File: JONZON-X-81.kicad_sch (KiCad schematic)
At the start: 30 parts, among them SW1 SW_DIP_x03, U1 AY-3-8910, U2 74HCT74, U3 74HCT08, U4 74HCT11, U5 74HCT02

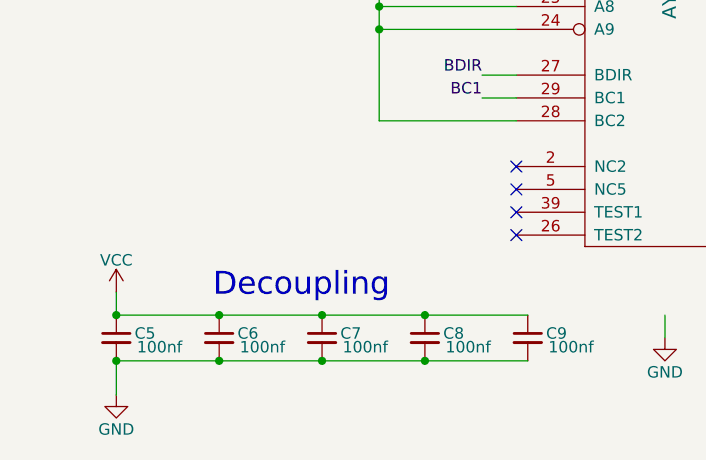
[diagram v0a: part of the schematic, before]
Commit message: Renamed files Added Ground and Audio Ground Planes Moved Ground Bridge to be between ground planes Generated some new images
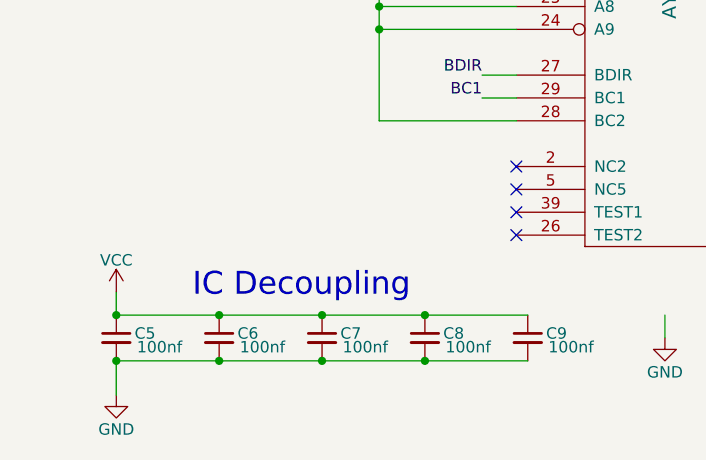
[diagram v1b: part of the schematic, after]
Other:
- note added: "IC Decoupling"
- note removed: "Decoupling"
- title: JonZON-X -> JONZON-X-81
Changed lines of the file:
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@@
 	(paper "A4")
 	(title_block
-		(title "JonZON-X")
+		(title "JONZON-X-81")
 		(date "2025-08-01")
 		(rev "1.0")
@@
 		)
 	)
-	(text "Decoupling"
+	(text "IC Decoupling"
 		(exclude_from_sim no)
 		(at 43.434 178.308 0)

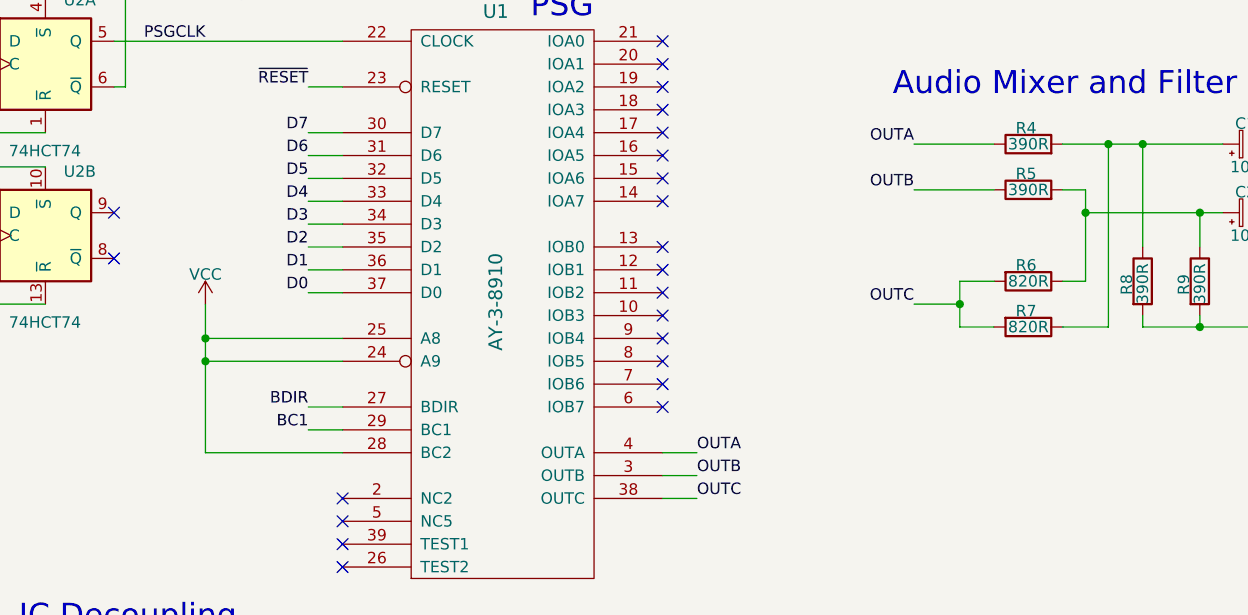
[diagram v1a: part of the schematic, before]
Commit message: Pulled /A9 low
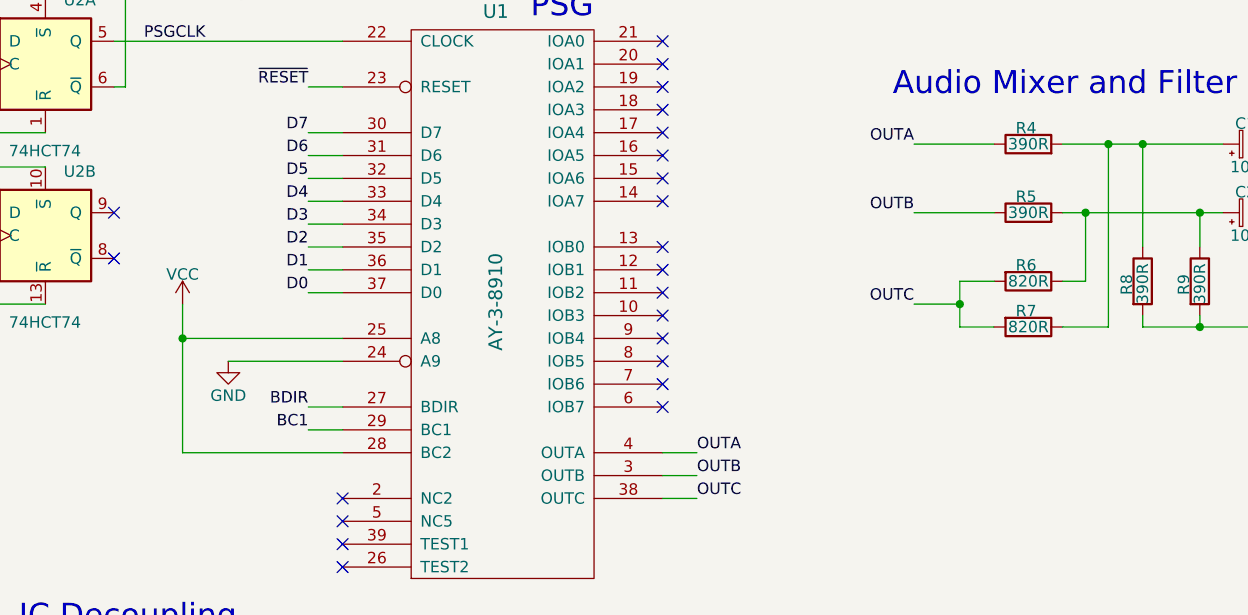
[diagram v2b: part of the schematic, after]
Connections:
- net GND: now also U1.24 (A9)
- net VCC: no longer U1.24 (A9)
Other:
- moved on the sheet: R5
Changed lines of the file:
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@@
 	)
 	(junction
-		(at 52.07 149.86)
-		(diameter 0)
-		(color 0 0 0 0)
-	)
-	(junction
 		(at 260.35 121.92)
 		(diameter 0)
@@
 	)
 	(junction
-		(at 52.07 147.32)
-		(diameter 0)
-		(color 0 0 0 0)
-	)
-	(junction
 		(at 90.17 31.75)
 		(diameter 0)
@@
 	)
 	(junction
+		(at 49.53 147.32)
+		(diameter 0)
+		(color 0 0 0 0)
+	)
+	(junction
 		(at 24.13 135.89)
 		(diameter 0)
@@
 	(wire
 		(pts
-			(xy 69.85 82.55) (xy 64.77 82.55)
+			(xy 54.61 149.86) (xy 67.31 149.86)
 		)
 		(stroke
@@
 	(wire
 		(pts
-			(xy 130.81 46.99) (xy 135.89 46.99)
+			(xy 69.85 82.55) (xy 64.77 82.55)
 		)
 		(stroke
@@
 	(wire
 		(pts
-			(xy 147.32 125.73) (xy 152.4 125.73)
+			(xy 130.81 46.99) (xy 135.89 46.99)
 		)
 		(stroke
@@
 	(wire
 		(pts
-			(xy 22.86 181.61) (xy 34.29 181.61)
+			(xy 147.32 125.73) (xy 152.4 125.73)
 		)
 		(stroke
@@
 	(wire
 		(pts
-			(xy 163.83 35.56) (xy 166.37 35.56)
+			(xy 22.86 181.61) (xy 34.29 181.61)
 		)
 		(stroke
@@
 	(wire
 		(pts
-			(xy 26.67 67.31) (xy 31.75 67.31)
+			(xy 163.83 35.56) (xy 166.37 35.56)
 		)
 		(stroke
@@
 	(wire
 		(pts
-			(xy 26.67 133.35) (xy 24.13 133.35)
+			(xy 26.67 67.31) (xy 31.75 67.31)
 		)
 		(stroke
@@
 	(wire
 		(pts
-			(xy 52.07 149.86) (xy 67.31 149.86)
+			(xy 26.67 133.35) (xy 24.13 133.35)
 		)
 		(stroke
@@
 	(wire
 		(pts
+			(xy 130.81 133.35) (xy 139.7 133.35)
+		)
+		(stroke
+			(width 0)
+			(type default)
+		)
+	)
+	(wire
+		(pts
 			(xy 162.56 133.35) (xy 165.1 133.35)
 		)
@@
 	(wire
 		(pts
-			(xy 52.07 147.32) (xy 67.31 147.32)
-		)
-		(stroke
-			(width 0)
-			(type default)
-		)
-	)
-	(wire
-		(pts
 			(xy 255.27 35.56) (xy 255.27 40.64)
 		)
@@
 	(wire
 		(pts
-			(xy 149.86 133.35) (xy 149.86 130.81)
-		)
-		(stroke
-			(width 0)
-			(type default)
-		)
-	)
-	(wire
-		(pts
 			(xy 156.21 144.78) (xy 156.21 146.05)
 		)
@@
 	(wire
 		(pts
-			(xy 52.07 147.32) (xy 52.07 149.86)
+			(xy 49.53 147.32) (xy 49.53 160.02)
 		)
 		(stroke
@@
 	(wire
 		(pts
-			(xy 52.07 160.02) (xy 67.31 160.02)
+			(xy 49.53 160.02) (xy 67.31 160.02)
 		)
 		(stroke
@@
 	(wire
 		(pts
-			(xy 130.81 130.81) (xy 139.7 130.81)
-		)
-		(stroke
-			(width 0)
-			(type default)
-		)
-	)
-	(wire
-		(pts
 			(xy 17.78 116.84) (xy 26.67 116.84)
 		)
@@
 	(wire
 		(pts
-			(xy 52.07 143.51) (xy 52.07 147.32)
+			(xy 49.53 143.51) (xy 49.53 147.32)
 		)
 		(stroke
@@
 	(wire
 		(pts
-			(xy 147.32 130.81) (xy 149.86 130.81)
+			(xy 147.32 133.35) (xy 149.86 133.35)
 		)
 		(stroke
@@
 	(wire
 		(pts
-			(xy 52.07 149.86) (xy 52.07 160.02)
+			(xy 203.2 125.73) (xy 195.58 125.73)
 		)
 		(stroke
@@
 	(wire
 		(pts
-			(xy 203.2 125.73) (xy 195.58 125.73)
+			(xy 139.7 140.97) (xy 135.89 140.97)
 		)
 		(stroke
@@
 	(wire
 		(pts
-			(xy 139.7 140.97) (xy 135.89 140.97)
+			(xy 76.2 31.75) (xy 71.12 31.75)
 		)
 		(stroke
@@
 	(wire
 		(pts
-			(xy 76.2 31.75) (xy 71.12 31.75)
+			(xy 49.53 147.32) (xy 67.31 147.32)
 		)
 		(stroke
@@
 	)
 	(label "OUTB"
-		(at 130.81 130.81 180)
+		(at 130.81 133.35 180)
 		(effects
 			(font
@@
 		(lib_name "R_6")
 		(lib_id "Device:R")
-		(at 143.51 130.81 90)
+		(at 143.51 133.35 90)
 		(unit 1)
 		(exclude_from_sim no)
@@
 		(dnp no)
 		(property "Reference" "R5"
-			(at 143.256 129.032 90)
+			(at 143.256 131.572 90)
 			(effects
 				(font
@@
 		)
 		(property "Value" "390R"
-			(at 143.51 130.81 90)
+			(at 143.51 133.35 90)
 			(effects
 				(font
@@
 		)
 		(property "Footprint" "Resistor_THT:R_Axial_DIN0207_L6.3mm_D2.5mm_P7.62mm_Horizontal"
-			(at 143.51 132.588 90)
+			(at 143.51 135.128 90)
 			(effects
 				(font
@@
 		)
 		(property "Datasheet" "~"
-			(at 143.51 130.81 0)
+			(at 143.51 133.35 0)
 			(effects
 				(font
@@
 		)
 		(property "Description" "Resistor"
-			(at 143.51 130.81 0)
+			(at 143.51 133.35 0)
 			(effects
 				(font
@@
 	(symbol
 		(lib_id "power:VCC")
-		(at 52.07 143.51 0)
+		(at 49.53 143.51 0)
 		(unit 1)
 		(exclude_from_sim no)
@@
 		(dnp no)
 		(property "Reference" "#PWR03"
-			(at 52.07 147.32 0)
+			(at 49.53 147.32 0)
 			(effects
 				(font
@@
 		)
 		(property "Value" "VCC"
-			(at 52.07 140.208 0)
+			(at 49.53 140.208 0)
 			(effects
 				(font
@@
 		)
 		(property "Footprint" ""
-			(at 52.07 143.51 0)
+			(at 49.53 143.51 0)
 			(effects
 				(font
@@
 		)
 		(property "Datasheet" ""
-			(at 52.07 143.51 0)
+			(at 49.53 143.51 0)
 			(effects
 				(font
@@
 		)
 		(property "Description" "Power symbol creates a global label with name \"VCC\""
-			(at 52.07 143.51 0)
+			(at 49.53 143.51 0)
 			(effects
 				(font
@@
 					(unit 1)
 				)
+			)
+		)
+	)
+	(symbol
+		(lib_id "power:GND")
+		(at 54.61 149.86 0)
+		(unit 1)
+		(exclude_from_sim no)
+		(in_bom yes)
+		(on_board yes)
+		(dnp no)
+		(property "Reference" "#PWR015"
+			(at 54.61 156.21 0)
+			(effects
+				(font
+					(size 1.27 1.27)
+				)
+				(hide yes)
+			)
+		)
+		(property "Value" "GND"
+			(at 54.61 153.67 0)
+			(effects
+				(font
+					(size 1.27 1.27)
+				)
+			)
+		)
+		(property "Footprint" ""
+			(at 54.61 149.86 0)
+			(effects
+				(font
+					(size 1.27 1.27)
+				)
+				(hide yes)
+			)
+		)
+		(property "Datasheet" ""
+			(at 54.61 149.86 0)
+			(effects
+				(font
+					(size 1.27 1.27)
+				)
+				(hide yes)
+			)
+		)
+		(property "Description" "Power symbol creates a global label with name \"GND\" , ground"
+			(at 54.61 149.86 0)
+			(effects
+				(font
+					(size 1.27 1.27)
+				)
+				(hide yes)
+			)
+		)
+		(pin "1"
+		)
+		(instances
+			(project "JONZON-X-81"
+				(path "/84e03406-665a-4400-b991-4fa8ce9d51c9"
+					(reference "#PWR015")
+					(unit 1)
+				)

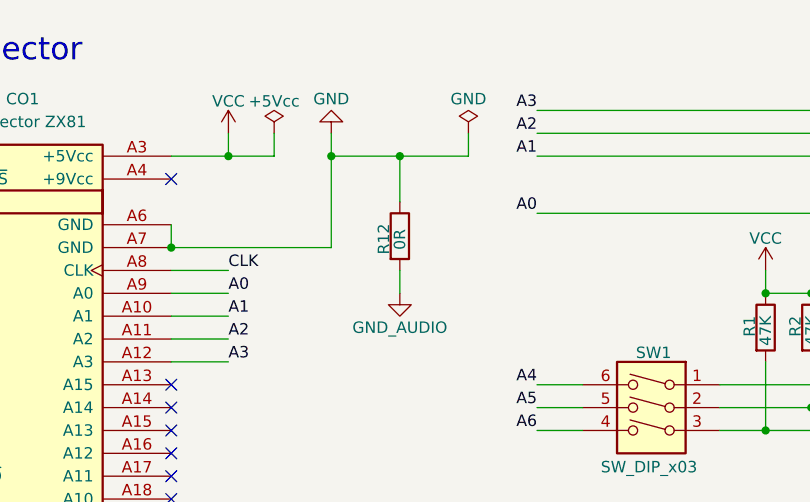
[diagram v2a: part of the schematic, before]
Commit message: fenced and stiched ground planes
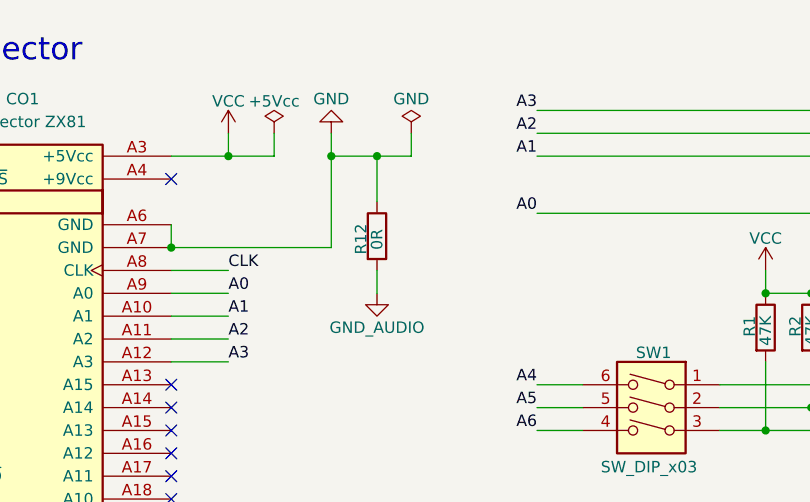
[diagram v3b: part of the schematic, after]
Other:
- moved on the sheet: R12
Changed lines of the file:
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@@
 	)
 	(junction
-		(at 260.35 121.92)
+		(at 87.63 31.75)
 		(diameter 0)
 		(color 0 0 0 0)
 	)
 	(junction
-		(at 90.17 31.75)
+		(at 260.35 121.92)
 		(diameter 0)
 		(color 0 0 0 0)
@@
 	(wire
 		(pts
-			(xy 90.17 31.75) (xy 97.79 31.75)
-		)
-		(stroke
-			(width 0)
-			(type default)
-		)
-	)
-	(wire
-		(pts
-			(xy 97.79 29.21) (xy 97.79 31.75)
+			(xy 91.44 29.21) (xy 91.44 31.75)
 		)
 		(stroke
@@
 	(wire
 		(pts
-			(xy 90.17 44.45) (xy 90.17 46.99)
-		)
-		(stroke
-			(width 0)
-			(type default)
-		)
-	)
-	(wire
-		(pts
 			(xy 43.18 106.68) (xy 43.18 119.38)
 		)
@@
 	(wire
 		(pts
-			(xy 90.17 31.75) (xy 90.17 36.83)
+			(xy 87.63 31.75) (xy 87.63 36.83)
 		)
 		(stroke
@@
 	(wire
 		(pts
+			(xy 87.63 31.75) (xy 91.44 31.75)
+		)
+		(stroke
+			(width 0)
+			(type default)
+		)
+	)
+	(wire
+		(pts
 			(xy 193.04 124.46) (xy 193.04 133.35)
 		)
@@
 	(wire
 		(pts
-			(xy 82.55 31.75) (xy 90.17 31.75)
+			(xy 82.55 31.75) (xy 87.63 31.75)
 		)
 		(stroke
@@
 	(wire
 		(pts
+			(xy 87.63 44.45) (xy 87.63 46.99)
+		)
+		(stroke
+			(width 0)
+			(type default)
+		)
+	)
+	(wire
+		(pts
 			(xy 106.68 162.56) (xy 102.87 162.56)
 		)
@@
 	(symbol
 		(lib_id "power:GND")
-		(at 90.17 46.99 0)
+		(at 87.63 46.99 0)
 		(unit 1)
 		(exclude_from_sim no)
@@
 		(dnp no)
 		(property "Reference" "#PWR014"
-			(at 90.17 53.34 0)
+			(at 87.63 53.34 0)
 			(effects
 				(font
@@
 		)
 		(property "Value" "GND_AUDIO"
-			(at 90.17 50.8 0)
+			(at 87.63 50.8 0)
 			(effects
 				(font
@@
 		)
 		(property "Footprint" ""
-			(at 90.17 46.99 0)
+			(at 87.63 46.99 0)
 			(effects
 				(font
@@
 		)
 		(property "Datasheet" ""
-			(at 90.17 46.99 0)
+			(at 87.63 46.99 0)
 			(effects
 				(font
@@
 		)
 		(property "Description" "Power symbol creates a global label with name \"GND\" , ground"
-			(at 90.17 46.99 0)
+			(at 87.63 46.99 0)
 			(effects
 				(font
@@
 	(symbol
 		(lib_id "power:PWR_FLAG")
-		(at 97.79 29.21 0)
+		(at 91.44 29.21 0)
 		(unit 1)
 		(exclude_from_sim no)
@@
 		(dnp no)
 		(property "Reference" "#FLG03"
-			(at 97.79 27.305 0)
+			(at 91.44 27.305 0)
 			(effects
 				(font
@@
 		)
 		(property "Value" "GND"
-			(at 97.79 25.4 0)
+			(at 91.44 25.4 0)
 			(effects
 				(font
@@
 		)
 		(property "Footprint" ""
-			(at 97.79 29.21 0)
+			(at 91.44 29.21 0)
 			(effects
 				(font
@@
 		)
 		(property "Datasheet" "~"
-			(at 97.79 29.21 0)
+			(at 91.44 29.21 0)
 			(effects
 				(font
@@
 		)
 		(property "Description" "Special symbol for telling ERC where power comes from"
-			(at 97.79 29.21 0)
+			(at 91.44 29.21 0)
 			(effects
 				(font
@@
 	(symbol
 		(lib_id "Device:R")
-		(at 90.17 40.64 0)
+		(at 87.63 40.64 0)
 		(unit 1)
 		(exclude_from_sim no)
@@
 		(dnp no)
 		(property "Reference" "R12"
-			(at 88.392 42.672 90)
+			(at 85.852 42.672 90)
 			(effects
 				(font
@@
 		)
 		(property "Value" "0R"
-			(at 90.17 42.164 90)
+			(at 87.63 42.164 90)
 			(effects
 				(font
@@
 		)
 		(property "Footprint" "Resistor_THT:R_Axial_DIN0207_L6.3mm_D2.5mm_P7.62mm_Horizontal"
-			(at 88.392 40.64 90)
+			(at 85.852 40.64 90)
 			(effects
 				(font
@@
 		)
 		(property "Datasheet" "~"
-			(at 90.17 40.64 0)
+			(at 87.63 40.64 0)
 			(effects
 				(font
@@
 		)
 		(property "Description" "Resistor"
-			(at 90.17 40.64 0)
+			(at 87.63 40.64 0)
 			(effects
 				(font

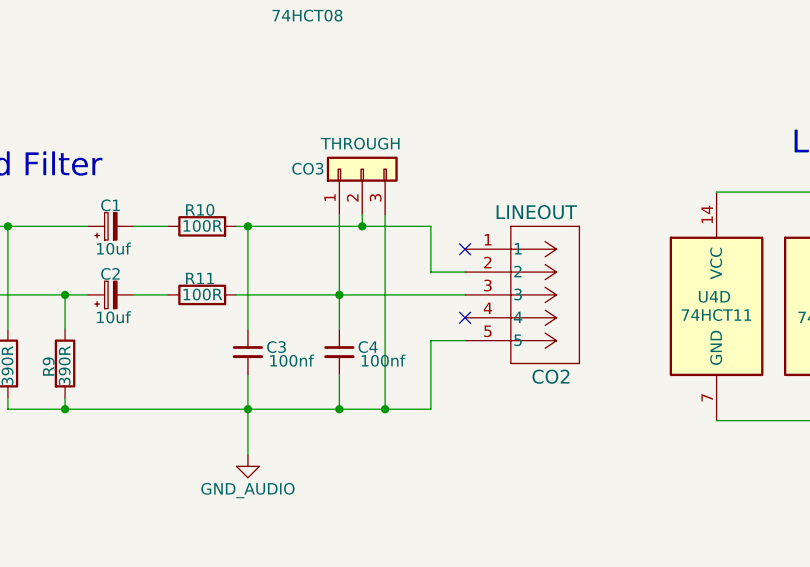
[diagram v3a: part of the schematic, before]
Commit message: corrected connections on audio jack as the footprint does not match the schematic symbol pinout. the left and right where on rev 1.0 connected to shunts a and b. to correct this I will just place shorts between pins 3 and 4 and 1 and 2 when the rev 1.0 boards arrive.
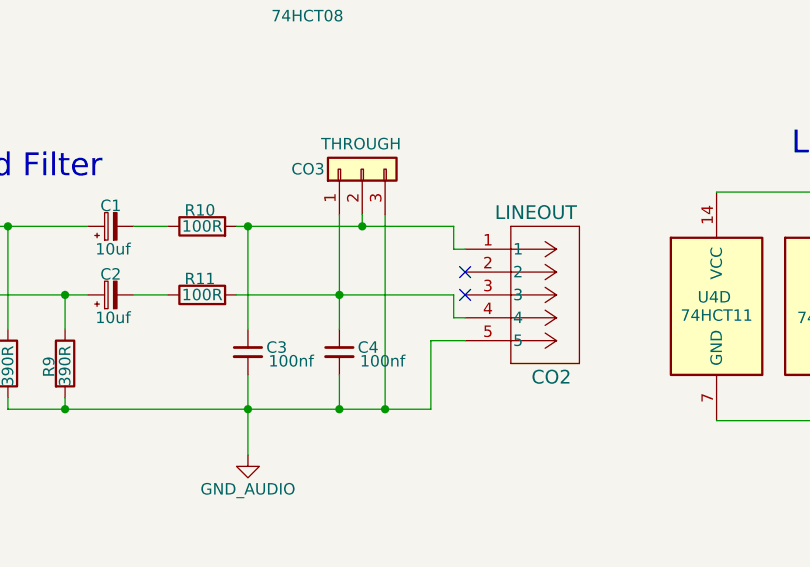
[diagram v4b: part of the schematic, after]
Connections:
- net at C4.1, CO3.1 (Pin_1), R11.2: now also CO2.4; no longer CO2.3
- net at C3.1, CO3.2 (Pin_2), R10.2: now also CO2.1; no longer CO2.2
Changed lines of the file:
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@@
 		(title "JONZON-X-81")
 		(date "2025-08-01")
-		(rev "1.0")
+		(rev "1.1")
 	)
 	(text "Address Decoding with DIP Switch Options \nfor PSG select addresses of A4,5 and 6 \nto allow up to 3 PSG's for up to 9 channel sound"
@@
 	)
 	(no_connect
+		(at 207.01 130.81)
+	)
+	(no_connect
 		(at 31.75 87.63)
 	)
@@
 	)
 	(no_connect
-		(at 207.01 135.89)
-	)
-	(no_connect
 		(at 102.87 119.38)
 	)
@@
 	)
 	(no_connect
-		(at 207.01 128.27)
-	)
-	(no_connect
 		(at 31.75 80.01)
 	)
@@
 	)
 	(no_connect
+		(at 207.01 133.35)
+	)
+	(no_connect
 		(at 64.77 72.39)
 	)
@@
 	(wire
 		(pts
+			(xy 203.2 138.43) (xy 207.01 138.43)
+		)
+		(stroke
+			(width 0)
+			(type default)
+		)
+	)
+	(wire
+		(pts
 			(xy 149.86 140.97) (xy 149.86 133.35)
 		)
@@
 	(wire
 		(pts
-			(xy 193.04 133.35) (xy 207.01 133.35)
-		)
-		(stroke
-			(width 0)
-			(type default)
-		)
-	)
-	(wire
-		(pts
 			(xy 63.5 124.46) (xy 67.31 124.46)
 		)
@@
 	(wire
 		(pts
+			(xy 205.74 125.73) (xy 205.74 128.27)
+		)
+		(stroke
+			(width 0)
+			(type default)
+		)
+	)
+	(wire
+		(pts
 			(xy 64.77 41.91) (xy 82.55 41.91)
 		)
@@
 	(wire
 		(pts
-			(xy 207.01 138.43) (xy 203.2 138.43)
-		)
-		(stroke
-			(width 0)
-			(type default)
-		)
-	)
-	(wire
-		(pts
-			(xy 203.2 130.81) (xy 207.01 130.81)
-		)
-		(stroke
-			(width 0)
-			(type default)
-		)
-	)
-	(wire
-		(pts
 			(xy 135.89 59.69) (xy 146.05 59.69)
 		)
@@
 	(wire
 		(pts
-			(xy 203.2 130.81) (xy 203.2 125.73)
-		)
-		(stroke
-			(width 0)
-			(type default)
-		)
-	)
-	(wire
-		(pts
 			(xy 69.85 80.01) (xy 64.77 80.01)
 		)
@@
 	(wire
 		(pts
+			(xy 205.74 128.27) (xy 207.01 128.27)
+		)
+		(stroke
+			(width 0)
+			(type default)
+		)
+	)
+	(wire
+		(pts
 			(xy 49.53 160.02) (xy 67.31 160.02)
 		)
@@
 	(wire
 		(pts
+			(xy 205.74 133.35) (xy 193.04 133.35)
+		)
+		(stroke
+			(width 0)
+			(type default)
+		)
+	)
+	(wire
+		(pts
 			(xy 26.67 54.61) (xy 31.75 54.61)
 		)
@@
 	(wire
 		(pts
+			(xy 207.01 135.89) (xy 205.74 135.89)
+		)
+		(stroke
+			(width 0)
+			(type default)
+		)
+	)
+	(wire
+		(pts
 			(xy 162.56 146.05) (xy 182.88 146.05)
 		)
@@
 	(wire
 		(pts
+			(xy 205.74 135.89) (xy 205.74 133.35)
+		)
+		(stroke
+			(width 0)
+			(type default)
+		)
+	)
+	(wire
+		(pts
 			(xy 135.89 146.05) (xy 139.7 146.05)
 		)
@@
 	(wire
 		(pts
-			(xy 203.2 125.73) (xy 195.58 125.73)
-		)
-		(stroke
+			(xy 195.58 125.73) (xy 205.74 125.73)
+		)
+		(stroke

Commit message: updated rev 1.1 and readme.
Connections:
- net OUTA: now also R5.1; no longer R4.1
- net OUTB: now also R4.1; no longer R5.1
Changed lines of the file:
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@@
 		)
 	)
-	(label "OUTB"
+	(label "OUTA"
 		(at 130.81 133.35 180)
 		(effects
@@
 		)
 	)
-	(label "OUTA"
+	(label "OUTB"
 		(at 130.81 125.73 180)
 		(effects

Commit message: 1.2
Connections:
- net OUTB: now also R6.2, R7.2; no longer R4.1
- net OUTC: now also R4.1; no longer R6.2, R7.2
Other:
- note added: "Channel A is Left Channel C is right Channel B (normaly noise on ZON-X) is mixed"
- note removed: "Channel A is Left Channel B is right Channel C (normaly noise) is mixed"
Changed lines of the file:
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@@
 		(title "JONZON-X-81")
 		(date "2025-08-01")
-		(rev "1.1")
+		(rev "1.2")
 	)
 	(text "Address Decoding with DIP Switch Options \nfor PSG select addresses of A4,5 and 6 \nto allow up to 3 PSG's for up to 9 channel sound"
@@
 	(text "BDIR	BC1\n0		0					INACTIVE\n0		1	/IORD	XX0FH	READ PSG\n1		0	/IORW	XX0FH	WRITE PSG\n1		1	/IOWR	XXDFH	LATCH ADDRESS\n\n			XX0FH = 0FH = 00001111\n			XXDFH = DFH = 10001111"
 		(exclude_from_sim no)
-		(at 203.962 173.736 0)
+		(at 206.756 171.958 0)
 		(effects
 			(font
@@
 		)
 	)
-	(text "Channel A is Left\nChannel B is right\nChannel C (normaly noise) is mixed"
+	(text "Channel A is Left\nChannel C is right\nChannel B (normaly noise on ZON-X) is mixed"
 		(exclude_from_sim no)
-		(at 178.562 170.688 0)
+		(at 177.8 168.91 0)
 		(effects
 			(font
@@
 		)
 	)
-	(label "OUTC"
+	(label "OUTB"
 		(at 130.81 143.51 180)
 		(effects
@@
 		)
 	)
-	(label "OUTB"
+	(label "OUTC"
 		(at 130.81 125.73 180)
 		(effects
